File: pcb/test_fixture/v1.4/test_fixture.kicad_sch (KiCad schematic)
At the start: 54 parts, among them J2 SM03B-SRSS-TB_LF__SN_, J3 Conn_ARM_JTAG_SWD_10, Q1 NMOS, SW1 SW_SPDT, U2 MIC29302WU, U3 INA186A5IDCKR

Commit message: v1.4.52840 harness done
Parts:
- removed C1, C4: 1u, Resistor_SMD:R_1206_3216Metric, symbol Device:C
- removed C5, C8: 100n, Resistor_SMD:R_1206_3216Metric, symbol Device:C
- removed J2: SM03B-SRSS-TB_LF__SN_, df_footprints:JST_SM03B-SRSS-TB_LF__SN_, symbol SM03B-SRSS-TB_LF__SN_:SM03B-SRSS-TB_LF__SN_
- removed POGO13, POGO14: pogo, fixture:POGO, symbol Connector:Conn_01x01_Female
- removed R3: 0.04, Resistor_SMD:R_Shunt_Vishay_WSR2_WSR3_KelvinConnection, symbol Device:R
- removed U3: INA186A5IDCKR, SOT65P210X110-6N, symbol fixture:INA186A1IDCKR
- added GND, GND1, GND2: (no value), TestPoint:TestPoint_Pad_D1.5mm, symbol Connector:TestPoint
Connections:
- net BATT+ is gone; now on net VDD: BATT+1.1, POGO19.1 (Pin_1)
- net FF_Q is gone; now on net FF_Q_1.8: FF_Q1.1, POGO15.1 (Pin_1)
- net GND: now also GND.1, GND1.1, GND2.1
- net VREF_IN renamed VREF_IN_1.8

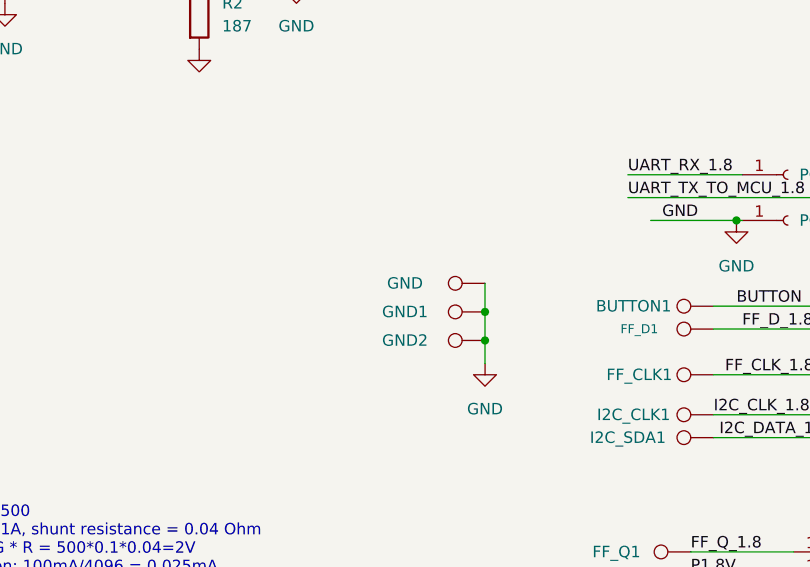
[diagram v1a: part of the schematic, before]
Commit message: Saving the first iteration of harness outputs
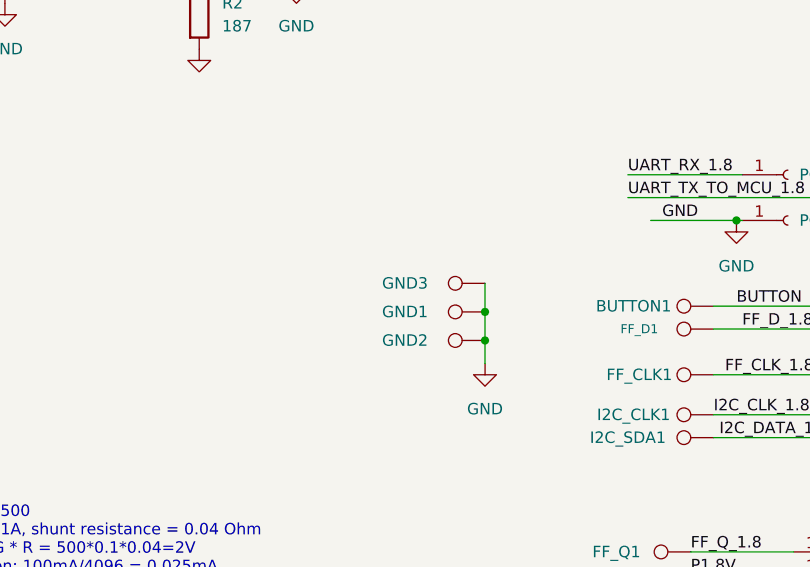
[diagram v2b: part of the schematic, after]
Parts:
- renumbered GND to GND3
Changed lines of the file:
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@@
   (symbol (lib_id "Connector:TestPoint") (at 232.41 74.93 90) (unit 1)
     (in_bom yes) (on_board yes) (dnp no)
-    (property "Reference" "GND" (at 223.52 74.93 90)
+    (property "Reference" "GND3" (at 223.52 74.93 90)
       (effects (font (size 1.27 1.27)))
     )
@@
       (project "test_fixture"
         (path "/e63e39d7-6ac0-4ffd-8aa3-1841a4541b55"
-          (reference "GND") (unit 1)
+          (reference "GND3") (unit 1)
         )
       )

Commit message: applied changes after placing engineering files for fixture to JLCPCB
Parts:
- Q1: LCSC (none) -> C916396
- R10: LCSC (none) -> C375503
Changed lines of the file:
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@@
+      (effects (font (size 1.27 1.27)) hide)
+    )
+    (property "Populate" "" (at 172.085 142.24 0)
+      (effects (font (size 1.27 1.27)) hide)
+    )
+    (property "LCSC" "C375503" (at 172.085 142.24 90)
       (effects (font (size 1.27 1.27)) hide)
     )
@@
       (effects (font (size 1.27 1.27)) hide)
     )
+    (property "Populate" "" (at 184.15 132.08 0)
+      (effects (font (size 1.27 1.27)) hide)
+    )
+    (property "LCSC" "C916396" (at 184.15 132.08 90)
+      (effects (font (size 1.27 1.27)) hide)
+    )
